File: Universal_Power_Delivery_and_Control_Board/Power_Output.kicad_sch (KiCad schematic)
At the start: 44 parts, among them CN1 B03B-XASK-1-A(LF)(SN), CN2 B03B-XASK-1-A(LF)(SN), CN3 B03B-XASK-1-A(LF)(SN), CN4 B03B-XASK-1-A(LF)(SN), CN5 XT30UPB-M, U10 SN74LVC1G17DCKR, U11 SN74LVC1G17DCKR, U12 SN74LVC1G17DCKR, U13 SN74LVC1G17DCKR, U14 SN74LVC1G17DCKR, U8 TPS51385RJNR, U9 TPS24751RUVR

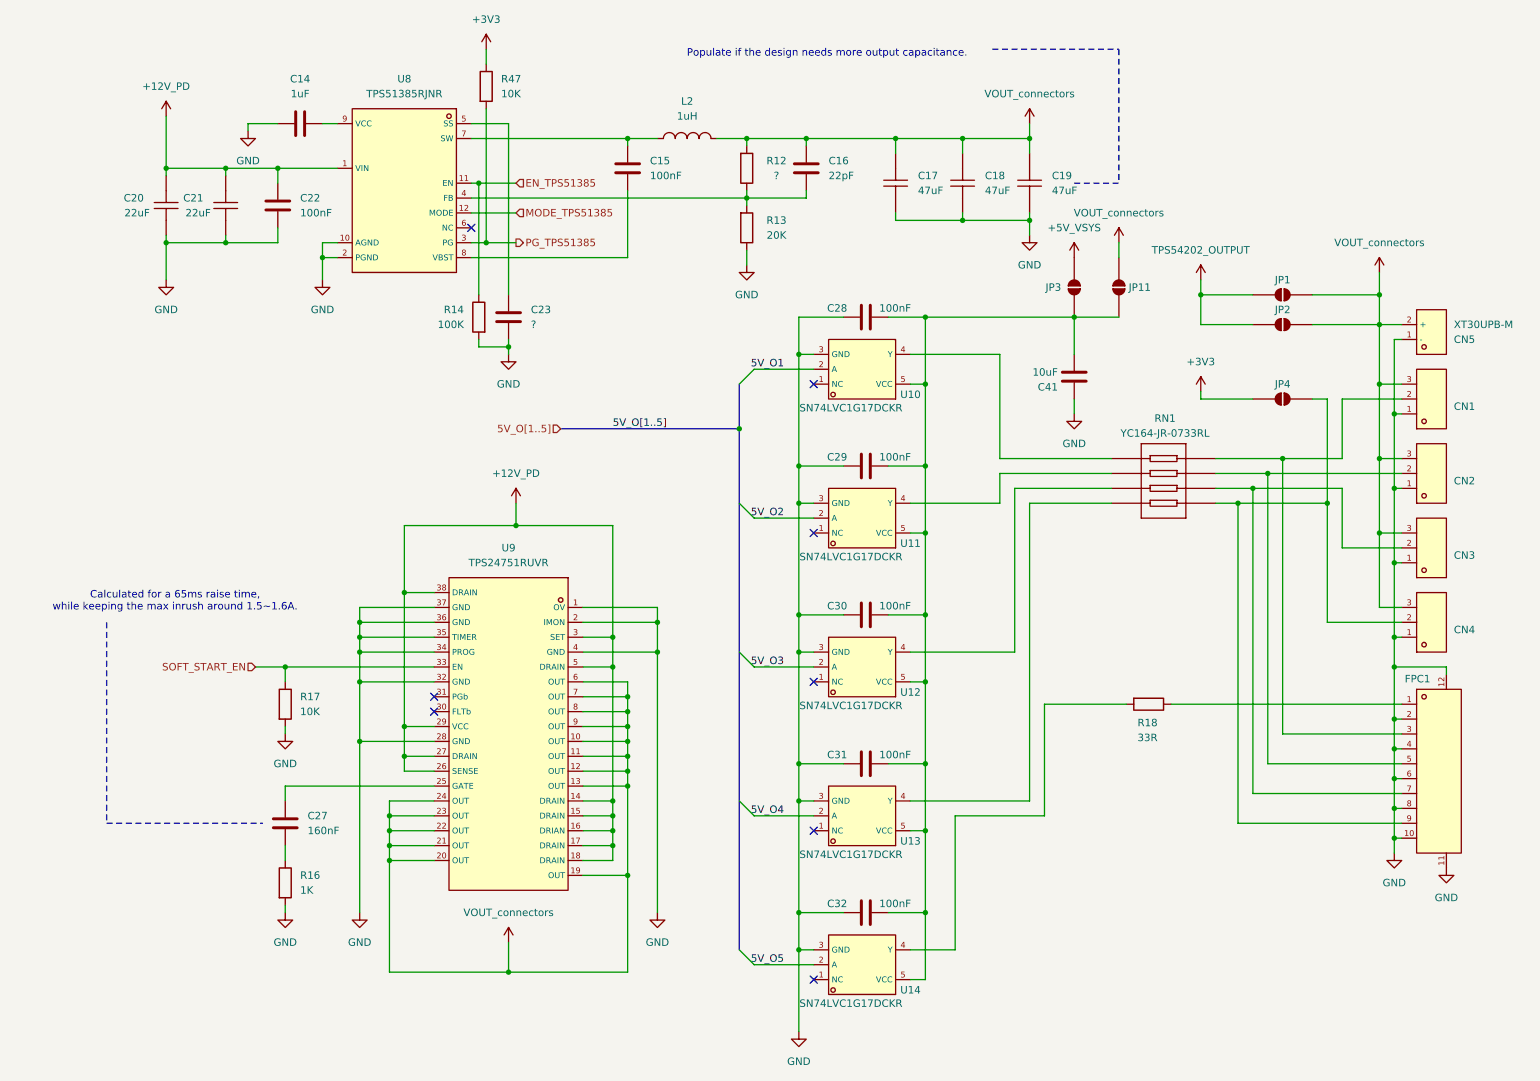
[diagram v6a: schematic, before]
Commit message: Small mostly cosmetic changes and reannotation of the schematic, followed by the export of the gerber files for production.
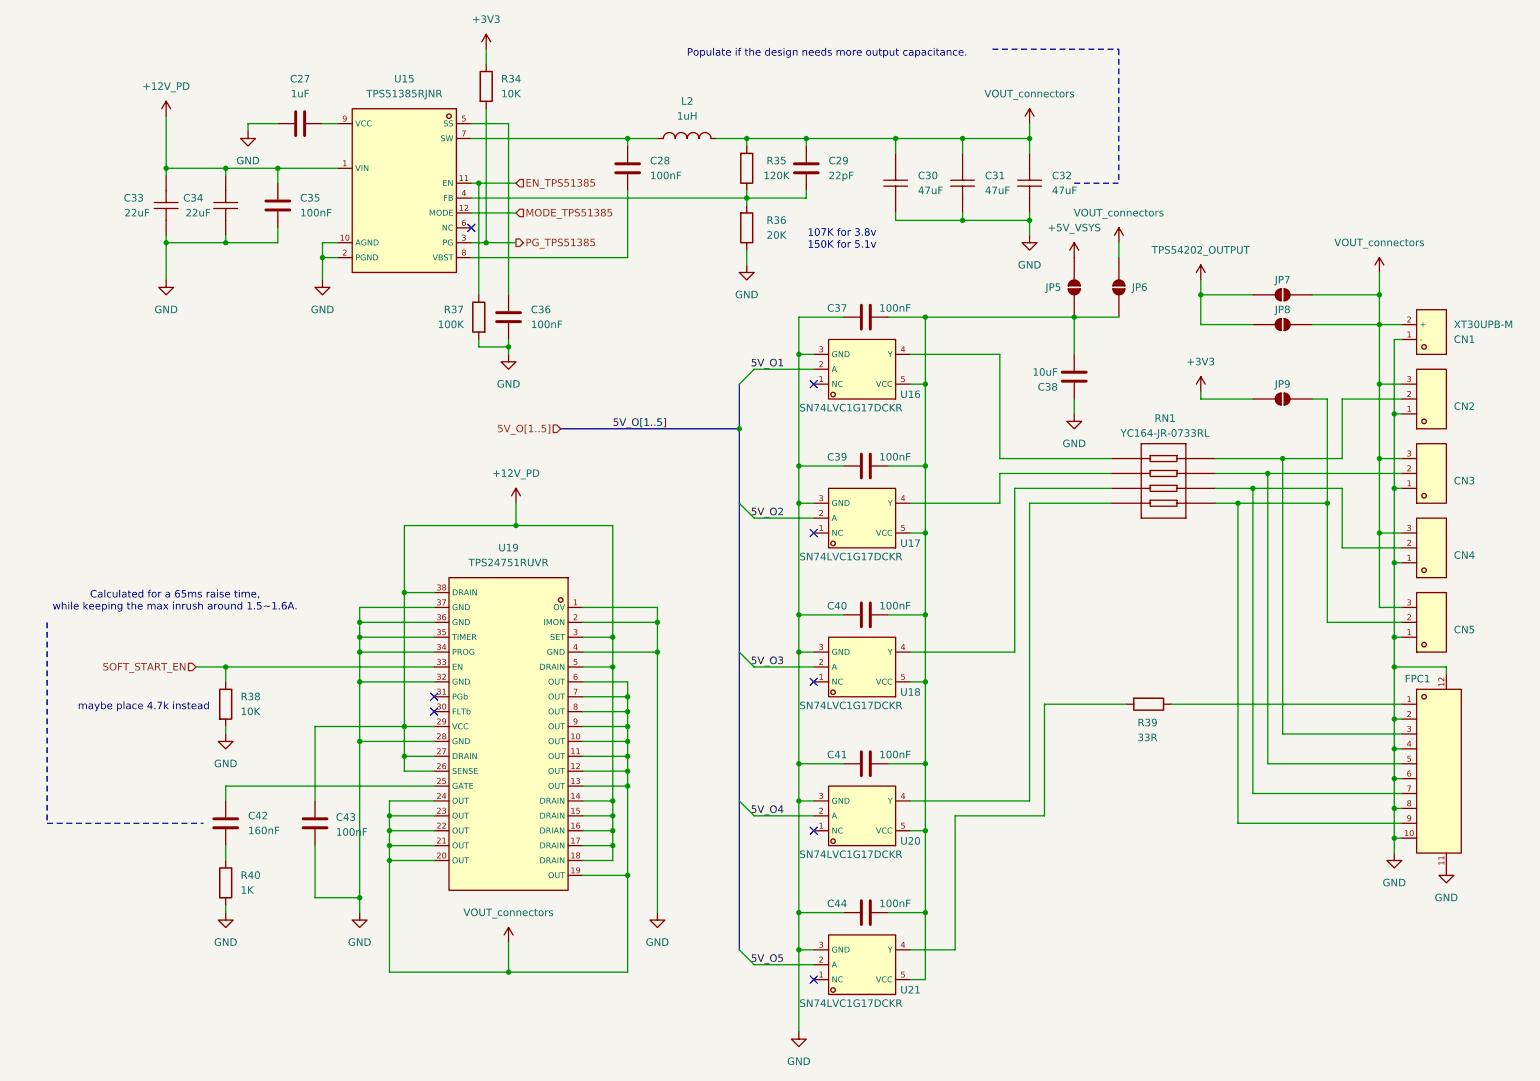
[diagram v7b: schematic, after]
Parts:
- added C43: 100nF, Capacitor_SMD:C_0402_1005Metric_Pad0.74x0.62mm_HandSolder, symbol Device:C
- C36: renamed from C23; value ? -> 100nF
- R35: renamed from R12; value ? -> 120K
- renumbered C14 to C27, C15 to C28, C16 to C29, C17 to C30, C18 to C31, C19 to C32, C20 to C33, C21 to C34, C22 to C35, C28 to C37, C41 to C38, C29 to C39, C30 to C40, C31 to C41, C27 to C42, C32 to C44, CN5 to CN1, CN1 to CN2, CN2 to CN3, CN3 to CN4, CN4 to CN5, JP3 to JP5, JP11 to JP6, JP1 to JP7, JP2 to JP8, JP4 to JP9, R47 to R34, R13 to R36, R14 to R37, R17 to R38, R18 to R39, R16 to R40, U8 to U15, U10 to U16, U11 to U17, U12 to U18, U9 to U19, U13 to U20, U14 to U21
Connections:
- net +12V_PD: now also C43.1
- net GND: now also C43.2
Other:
- note added: "107K for 3.8v 150K for 5.1v"
- note added: "maybe place 4.7k instead"
- company: (none) -> Jan Ścibielski
- title: (none) -> Power Output
- moved on the sheet: C42, R38, R40
